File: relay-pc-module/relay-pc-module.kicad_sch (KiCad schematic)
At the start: 55 parts, among them J1 Conn_02x02_Odd_Even, J10 Conn_01x01, J2 DB9_Female, J3 Conn_01x01, J4 Screw_Terminal_01x03, J5 Screw_Terminal_01x03, J6 Screw_Terminal_01x03, J7 Conn_01x04, J8 Conn_01x04, J9 Conn_01x01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

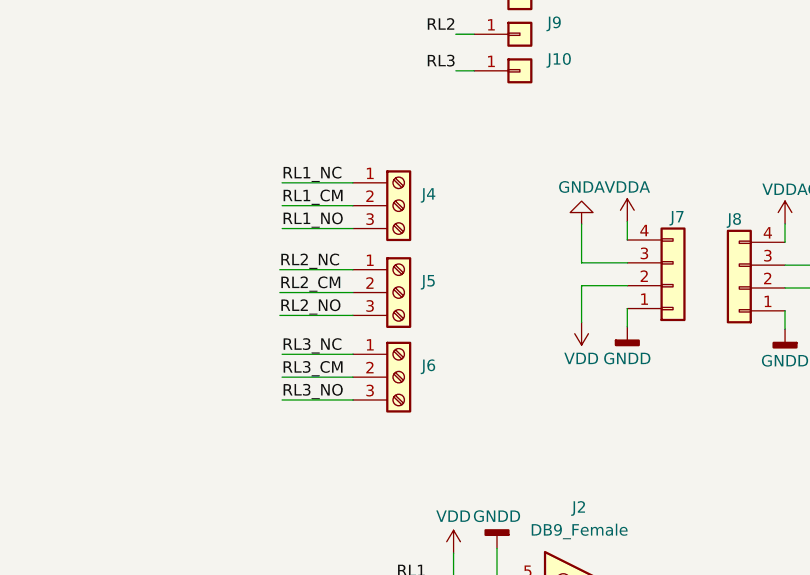
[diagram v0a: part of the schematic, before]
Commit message: Added 3D model and sim to relay precharge module
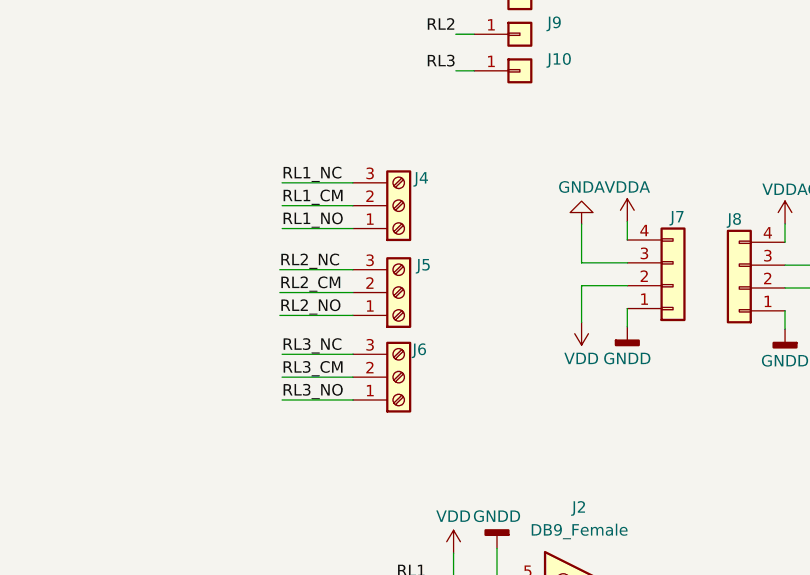
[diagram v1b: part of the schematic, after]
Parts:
- J4, J5, J6: footprint TerminalBlock:TerminalBlock_bornier-3_P5.08mm -> TerminalBlock_Phoenix:TerminalBlock_Phoenix_MKDS-1,5-3-5.08_1x03_P5.08mm_Horizontal
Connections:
- net RL1_NC: now also J4.3 (Pin_3); no longer J4.1 (Pin_1)
- net RL1_NO: now also J4.1 (Pin_1); no longer J4.3 (Pin_3)
- net RL2_NC: now also J5.3 (Pin_3); no longer J5.1 (Pin_1)
- net RL2_NO: now also J5.1 (Pin_1); no longer J5.3 (Pin_3)
- net RL3_NC: now also J6.3 (Pin_3); no longer J6.1 (Pin_1)
- net RL3_NO: now also J6.1 (Pin_1); no longer J6.3 (Pin_3)

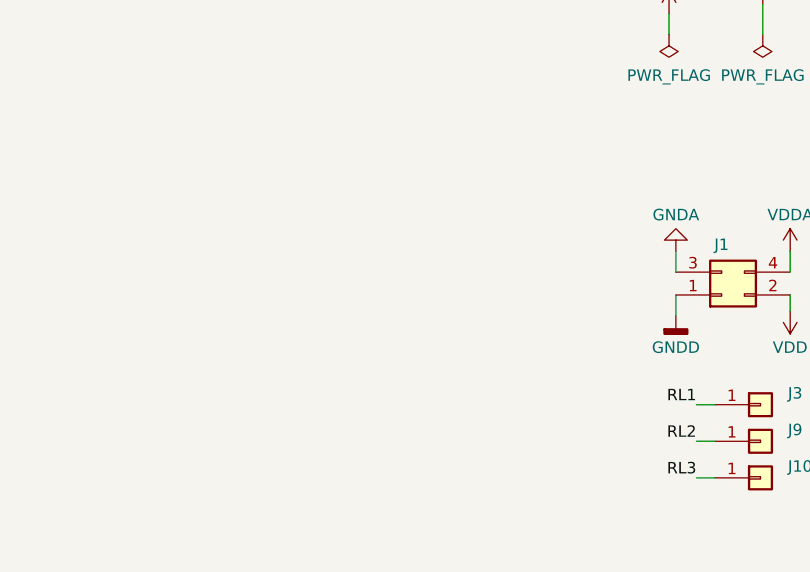
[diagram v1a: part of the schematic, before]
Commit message: Added LEDs to relay pc module
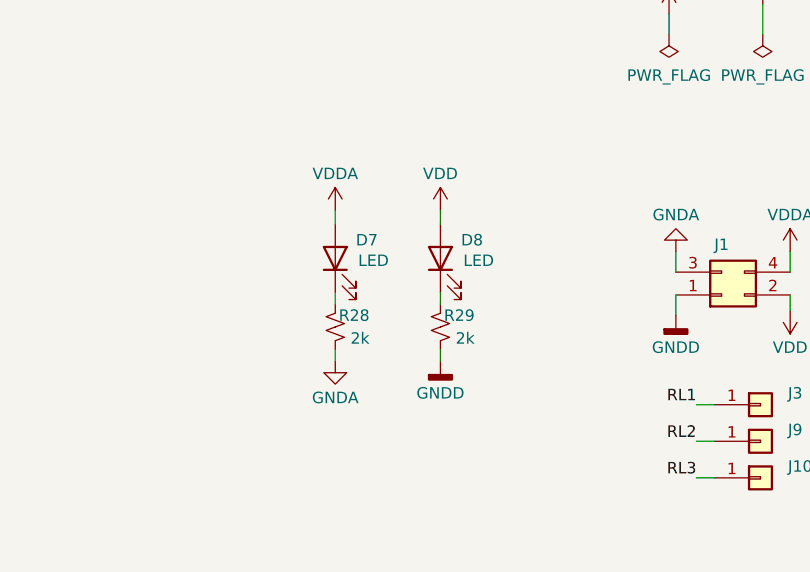
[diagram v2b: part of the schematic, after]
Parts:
- added D7, D8: LED, LED_SMD:LED_0805_2012Metric_Pad1.15x1.40mm_HandSolder, symbol Device:LED
- added R28, R29: 2k, Resistor_SMD:R_0805_2012Metric_Pad1.20x1.40mm_HandSolder, symbol Device:R_Small_US
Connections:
- net GNDA: now also R28.1
- net GNDD: now also R29.1
- net VDD: now also D8.2 (A)
- net VDDA: now also D7.2 (A)
- new net: D7.1 (K), R28.2
- new net: D8.1 (K), R29.2
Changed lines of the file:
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@@
+    (stroke (width 0) (type default) (color 0 0 0 0))
+  )
+  (wire (pts (xy 189.738 62.484) (xy 189.738 63.754))
     (stroke (width 0) (type default) (color 0 0 0 0))
   )
@@
     (stroke (width 0) (type default) (color 0 0 0 0))
   )
+  (wire (pts (xy 201.422 46.99) (xy 201.422 48.514))
+    (stroke (width 0) (type default) (color 0 0 0 0))
+  )
   (wire (pts (xy 36.83 80.01) (xy 35.56 80.01))
     (stroke (width 0) (type default) (color 0 0 0 0))
@@
     (stroke (width 0) (type default) (color 0 0 0 0))
   )
+  (wire (pts (xy 201.422 56.134) (xy 201.422 57.404))
+    (stroke (width 0) (type default) (color 0 0 0 0))
+  )
   (wire (pts (xy 226.568 135.89) (xy 235.966 135.89))
     (stroke (width 0) (type default) (color 0 0 0 0))
@@
     (stroke (width 0) (type default) (color 0 0 0 0))
   )
+  (wire (pts (xy 189.738 56.134) (xy 189.738 57.404))
+    (stroke (width 0) (type default) (color 0 0 0 0))
+  )
   (wire (pts (xy 35.052 29.464) (xy 35.052 30.226))
     (stroke (width 0) (type default) (color 0 0 0 0))
@@
     (stroke (width 0) (type default) (color 0 0 0 0))
   )
+  (wire (pts (xy 189.738 46.99) (xy 189.738 48.514))
+    (stroke (width 0) (type default) (color 0 0 0 0))
+  )
   (wire (pts (xy 80.01 138.684) (xy 96.52 138.684))
     (stroke (width 0) (type default) (color 0 0 0 0))
@@
   )
   (wire (pts (xy 53.34 102.87) (xy 53.34 101.6))
+    (stroke (width 0) (type default) (color 0 0 0 0))
+  )
+  (wire (pts (xy 201.422 62.484) (xy 201.422 63.754))
     (stroke (width 0) (type default) (color 0 0 0 0))
   )
@@
     (pin "3")
   )
+  (symbol (lib_id "power:GNDA") (at 189.738 63.754 0) (unit 1)
+    (in_bom yes) (on_board yes)
+    (property "Reference" "#PWR016" (id 0) (at 189.738 70.104 0)
+      (effects (font (size 1.27 1.27)) hide)
+    )
+    (property "Value" "GNDA" (id 1) (at 189.738 67.818 0))
+    (property "Footprint" "" (id 2) (at 189.738 63.754 0)
+      (effects (font (size 1.27 1.27)) hide)
+    )
+    (property "Datasheet" "" (id 3) (at 189.738 63.754 0)
+      (effects (font (size 1.27 1.27)) hide)
+    )
+    (pin "1")
+  )
   (symbol (lib_id "power:VDDA") (at 228.854 155.448 0) (mirror x) (unit 1)
     (in_bom yes) (on_board yes)
@@
     (pin "1")
     (pin "2")
+  )
+  (symbol (lib_id "Device:LED") (at 189.738 52.324 90) (unit 1)
+    (in_bom yes) (on_board yes)
+    (property "Reference" "D7" (id 0) (at 192.024 50.292 90)
+      (effects (font (size 1.27 1.27)) (justify right))
+    )
+    (property "Value" "LED" (id 1) (at 192.278 52.578 90)
+      (effects (font (size 1.27 1.27)) (justify right))
+    )
+    (property "Footprint" "LED_SMD:LED_0805_2012Metric_Pad1.15x1.40mm_HandSolder" (id 2) (at 189.738 52.324 0)
+      (effects (font (size 1.27 1.27)) hide)
+    )
+    (property "Datasheet" "~" (id 3) (at 189.738 52.324 0)
+      (effects (font (size 1.27 1.27)) hide)
+    )
+    (pin "1")
+    (pin "2")
+  )
+  (symbol (lib_id "Device:LED") (at 201.422 52.324 90) (unit 1)
+    (in_bom yes) (on_board yes)
+    (property "Reference" "D8" (id 0) (at 203.708 50.292 90)
+      (effects (font (size 1.27 1.27)) (justify right))
+    )
+    (property "Value" "LED" (id 1) (at 203.962 52.578 90)
+      (effects (font (size 1.27 1.27)) (justify right))
+    )
+    (property "Footprint" "LED_SMD:LED_0805_2012Metric_Pad1.15x1.40mm_HandSolder" (id 2) (at 201.422 52.324 0)
+      (effects (font (size 1.27 1.27)) hide)
+    )
+    (property "Datasheet" "~" (id 3) (at 201.422 52.324 0)
+      (effects (font (size 1.27 1.27)) hide)
+    )
+    (pin "1")
+    (pin "2")
+  )
+  (symbol (lib_id "power:GNDD") (at 201.422 63.754 0) (unit 1)
+    (in_bom yes) (on_board yes)
+    (property "Reference" "#PWR018" (id 0) (at 201.422 70.104 0)
+      (effects (font (size 1.27 1.27)) hide)
+    )
+    (property "Value" "GNDD" (id 1) (at 201.422 67.31 0))
+    (property "Footprint" "" (id 2) (at 201.422 63.754 0)
+      (effects (font (size 1.27 1.27)) hide)
+    )
+    (property "Datasheet" "" (id 3) (at 201.422 63.754 0)
+      (effects (font (size 1.27 1.27)) hide)
+    )
+    (pin "1")
   )
   (symbol (lib_id "Device:Q_NPN_BEC") (at 66.04 145.034 0) (unit 1)
@@
     (pin "3")
     (pin "4")
+  )
+  (symbol (lib_id "Device:R_Small_US") (at 201.422 59.944 0) (mirror x) (unit 1)
+    (in_bom yes) (on_board yes)
+    (property "Reference" "R29" (id 0) (at 205.232 58.674 0)
+      (effects (font (size 1.27 1.27)) (justify right))
+    )
+    (property "Value" "2k" (id 1) (at 205.232 61.214 0)
+      (effects (font (size 1.27 1.27)) (justify right))
+    )
+    (property "Footprint" "Resistor_SMD:R_0805_2012Metric_Pad1.20x1.40mm_HandSolder" (id 2) (at 201.422 59.944 0)
+      (effects (font (size 1.27 1.27)) hide)
+    )
+    (property "Datasheet" "~" (id 3) (at 201.422 59.944 0)
+      (effects (font (size 1.27 1.27)) hide)
+    )
+    (pin "1")
+    (pin "2")
   )
   (symbol (lib_id "Device:Q_NPN_BEC") (at 66.04 95.25 0) (unit 1)
@@
     (pin "2")
   )
+  (symbol (lib_id "power:VDDA") (at 189.738 46.99 0) (unit 1)
+    (in_bom yes) (on_board yes)
+    (property "Reference" "#PWR013" (id 0) (at 189.738 50.8 0)
+      (effects (font (size 1.27 1.27)) hide)
+    )
+    (property "Value" "VDDA" (id 1) (at 189.738 42.926 0))
+    (property "Footprint" "" (id 2) (at 189.738 46.99 0)
+      (effects (font (size 1.27 1.27)) hide)
+    )
+    (property "Datasheet" "" (id 3) (at 189.738 46.99 0)
+      (effects (font (size 1.27 1.27)) hide)
+    )
+    (pin "1")
+  )
   (symbol (lib_id "power:VDDA") (at 249.682 24.892 0) (unit 1)
     (in_bom yes) (on_board yes) (fields_autoplaced)
@@
     (pin "2")
     (pin "3")
+  )
+  (symbol (lib_id "power:VDD") (at 201.422 46.99 0) (mirror y) (unit 1)
+    (in_bom yes) (on_board yes)
+    (property "Reference" "#PWR015" (id 0) (at 201.422 50.8 0)
+      (effects (font (size 1.27 1.27)) hide)
+    )
+    (property "Value" "VDD" (id 1) (at 201.422 42.926 0))
+    (property "Footprint" "" (id 2) (at 201.422 46.99 0)
+      (effects (font (size 1.27 1.27)) hide)
+    )
+    (property "Datasheet" "" (id 3) (at 201.422 46.99 0)
+      (effects (font (size 1.27 1.27)) hide)
+    )
+    (pin "1")
   )
   (symbol (lib_id "power:VDD") (at 243.84 104.648 180) (unit 1)
@@
     (pin "2")
   )
+  (symbol (lib_id "Device:R_Small_US") (at 189.738 59.944 0) (mirror x) (unit 1)
+    (in_bom yes) (on_board yes)
+    (property "Reference" "R28" (id 0) (at 193.548 58.674 0)
+      (effects (font (size 1.27 1.27)) (justify right))
+    )
+    (property "Value" "2k" (id 1) (at 193.548 61.214 0)
+      (effects (font (size 1.27 1.27)) (justify right))
+    )
+    (property "Footprint" "Resistor_SMD:R_0805_2012Metric_Pad1.20x1.40mm_HandSolder" (id 2) (at 189.738 59.944 0)
+      (effects (font (size 1.27 1.27)) hide)
+    )
+    (property "Datasheet" "~" (id 3) (at 189.738 59.944 0)
+      (effects (font (size 1.27 1.27)) hide)
+    )
+    (pin "1")
+    (pin "2")
+  )
   (symbol (lib_id "Device:R_Small_US") (at 35.56 139.954 180) (unit 1)
     (in_bom yes) (on_board yes)
@@
       (reference "#PWR012") (unit 1) (value "GNDA") (footprint "")
     )
+    (path "/6ce69dde-e297-4692-b612-c13f4ef7f3e5"
+      (reference "#PWR013") (unit 1) (value "VDDA") (footprint "")
+    )
     (path "/4b19adca-5799-4906-8f75-10b9dc4356f2"
       (reference "#PWR014") (unit 1) (value "VDD") (footprint "")
     )
+    (path "/81999545-52f6-4be1-867a-8c57a6c5272d"
+      (reference "#PWR015") (unit 1) (value "VDD") (footprint "")
+    )
+    (path "/0ac5046d-95a0-4ce1-98f2-c194876b2140"
+      (reference "#PWR016") (unit 1) (value "GNDA") (footprint "")
+    )
     (path "/efc5e443-d470-49d7-8d68-428bbdad2c58"
       (reference "#PWR017") (unit 1) (value "GNDD") (footprint "")
     )
+    (path "/211e70cd-4168-436b-9a63-eaa08b67eb69"
+      (reference "#PWR018") (unit 1) (value "GNDD") (footprint "")
+    )
     (path "/35a2878d-6beb-4590-9c42-bd56751048da"
       (reference "#PWR019") (unit 1) (value "GNDA") (footprint "")
@@
       (reference "D6") (unit 1) (value "1N4148") (footprint "Diode_SMD:D_SOD-123")
     )
+    (path "/171090ec-af5c-495b-b4f9-a3b5778b8cc6"
+      (reference "D7") (unit 1) (value "LED") (footprint "LED_SMD:LED_0805_2012Metric_Pad1.15x1.40mm_HandSolder")
+    )
+    (path "/1d2e04a4-a2e3-4092-8c09-e8d0586b205c"
+      (reference "D8") (unit 1) (value "LED") (footprint "LED_SMD:LED_0805_2012Metric_Pad1.15x1.40mm_HandSolder")
+    )
     (path "/596f8946-9ca9-4ba3-9b29-4b2303057d02"
       (reference "J1") (unit 1) (value "Conn_02x02_Odd_Even") (footprint "Connector_PinHeader_2.54mm:PinHeader_2x02_P2.54mm_Vertical")
@@
       (reference "R27") (unit 1) (value "47k") (footprint "Resistor_SMD:R_0805_2012Metric_Pad1.20x1.40mm_HandSolder")
     )
+    (path "/bc293473-d4a7-47de-9585-79ef1759d23b"
+      (reference "R28") (unit 1) (value "2k") (footprint "Resistor_SMD:R_0805_2012Metric_Pad1.20x1.40mm_HandSolder")
+    )
+    (path "/456b7206-0c4e-4a9d-a425-3e2c24751fa4"
+      (reference "R29") (unit 1) (value "2k") (footprint "Resistor_SMD:R_0805_2012Metric_Pad1.20x1.40mm_HandSolder")
+    )
     (path "/60a847b6-4504-4664-a598-4351d9c62be2"

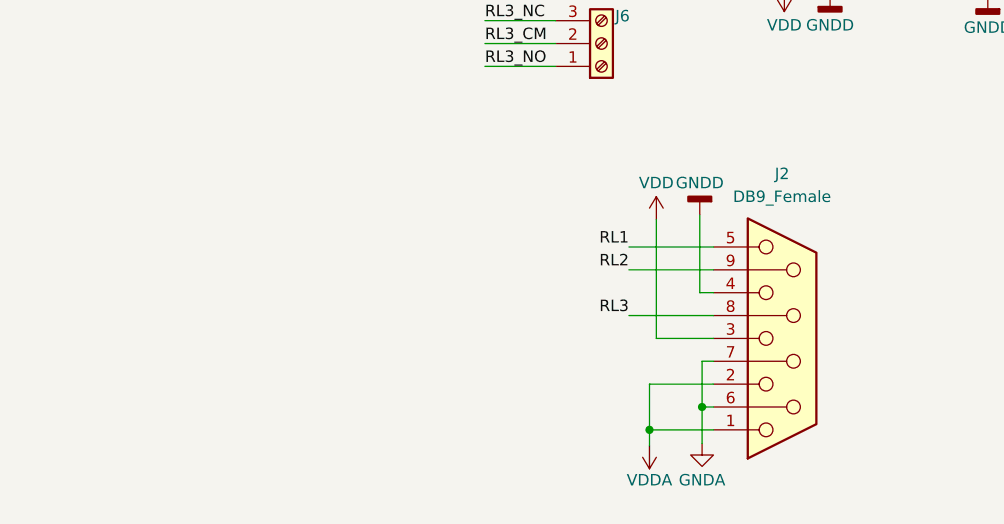
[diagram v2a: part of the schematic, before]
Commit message: Removed db9 connector from relay-pc module
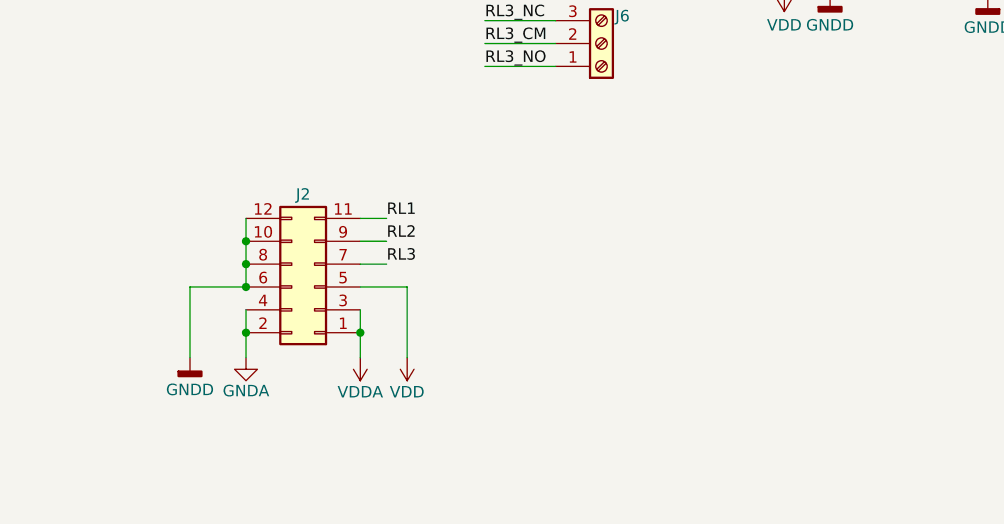
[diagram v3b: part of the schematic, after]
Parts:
- removed J2: DB9_Female, Connector_Dsub:DSUB-9_Female_Horizontal_P2.77x2.84mm_EdgePinOffset7.70mm_Housed_MountingHolesOffset9.12mm, symbol Connector:DB9_Female
- added J2: Conn_02x06_Odd_Even, Connector_PinHeader_2.54mm:PinHeader_2x06_P2.54mm_Horizontal, symbol Connector_Generic:Conn_02x06_Odd_Even
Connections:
- net GNDA: now also J2.2 (Pin_2), J2.4 (Pin_4)
- net GNDD: now also J2.10 (Pin_10), J2.12 (Pin_12), J2.6 (Pin_6), J2.8 (Pin_8)
- net RL1: now also J2.11 (Pin_11)
- net RL2: now also J2.9 (Pin_9)
- net RL3: now also J2.7 (Pin_7)
- net VDD: now also J2.5 (Pin_5)
- net VDDA: now also J2.1 (Pin_1), J2.3 (Pin_3)

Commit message: Inverter relay module connector
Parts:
- removed J10, J3, J9: Conn_01x01, Connector_PinHeader_2.54mm:PinHeader_1x01_P2.54mm_Vertical, symbol Connector_Generic:Conn_01x01
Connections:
- net GNDA: now also J2.10 (Pin_10), J2.12 (Pin_12); no longer J2.2 (Pin_2), J2.4 (Pin_4)
- net GNDD: now also J2.2 (Pin_2), J2.4 (Pin_4); no longer J2.10 (Pin_10), J2.12 (Pin_12)
- net RL1: now also J2.5 (Pin_5); no longer J2.11 (Pin_11)
- net RL2: now also J2.3 (Pin_3); no longer J2.9 (Pin_9)
- net RL3: now also J2.1 (Pin_1); no longer J2.7 (Pin_7)
- net VDD: now also J2.7 (Pin_7); no longer J2.5 (Pin_5)
- net VDDA: now also J2.11 (Pin_11), J2.9 (Pin_9); no longer J2.1 (Pin_1), J2.3 (Pin_3)
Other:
- moved on the sheet: J2

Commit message: Creted bom for relay module
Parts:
- R13, R22, R4: value 2k2 -> 2k
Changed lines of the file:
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@@
       (effects (font (size 1.27 1.27)) (justify right))
     )
-    (property "Value" "2k2" (id 1) (at 69.85 86.36 0)
+    (property "Value" "2k" (id 1) (at 69.85 86.36 0)
       (effects (font (size 1.27 1.27)) (justify right))
     )
@@
       (effects (font (size 1.27 1.27)) (justify right))
     )
-    (property "Value" "2k2" (id 1) (at 69.85 136.144 0)
+    (property "Value" "2k" (id 1) (at 69.85 136.144 0)
       (effects (font (size 1.27 1.27)) (justify right))
     )
@@
       (effects (font (size 1.27 1.27)) (justify right))
     )
-    (property "Value" "2k2" (id 1) (at 69.342 36.576 0)
+    (property "Value" "2k" (id 1) (at 69.342 36.576 0)
       (effects (font (size 1.27 1.27)) (justify right))
     )
@@
     )
     (path "/ee337fe5-5039-48ea-94c2-8a10f01a87c1"
-      (reference "R4") (unit 1) (value "2k2") (footprint "Resistor_SMD:R_0805_2012Metric_Pad1.20x1.40mm_HandSolder")
+      (reference "R4") (unit 1) (value "2k") (footprint "Resistor_SMD:R_0805_2012Metric_Pad1.20x1.40mm_HandSolder")
     )
     (path "/e3e1947a-3f5b-4820-94ab-7b12cc0d4b85"
@@
     )
     (path "/c446f748-9de5-4290-84d9-55196b68f00f"
-      (reference "R13") (unit 1) (value "2k2") (footprint "Resistor_SMD:R_0805_2012Metric_Pad1.20x1.40mm_HandSolder")
+      (reference "R13") (unit 1) (value "2k") (footprint "Resistor_SMD:R_0805_2012Metric_Pad1.20x1.40mm_HandSolder")
     )
     (path "/619eb7e5-3034-4d37-bac3-53adbd54921e"
@@
     )
     (path "/c6a7f0bd-64d5-4087-b086-755b57c9815f"
-      (reference "R22") (unit 1) (value "2k2") (footprint "Resistor_SMD:R_0805_2012Metric_Pad1.20x1.40mm_HandSolder")
+      (reference "R22") (unit 1) (value "2k") (footprint "Resistor_SMD:R_0805_2012Metric_Pad1.20x1.40mm_HandSolder")
     )
     (path "/bdfd26ff-6020-4125-849d-4ab318e88020"
